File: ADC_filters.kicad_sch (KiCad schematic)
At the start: 9 parts, among them U801 OPA356xxDBV

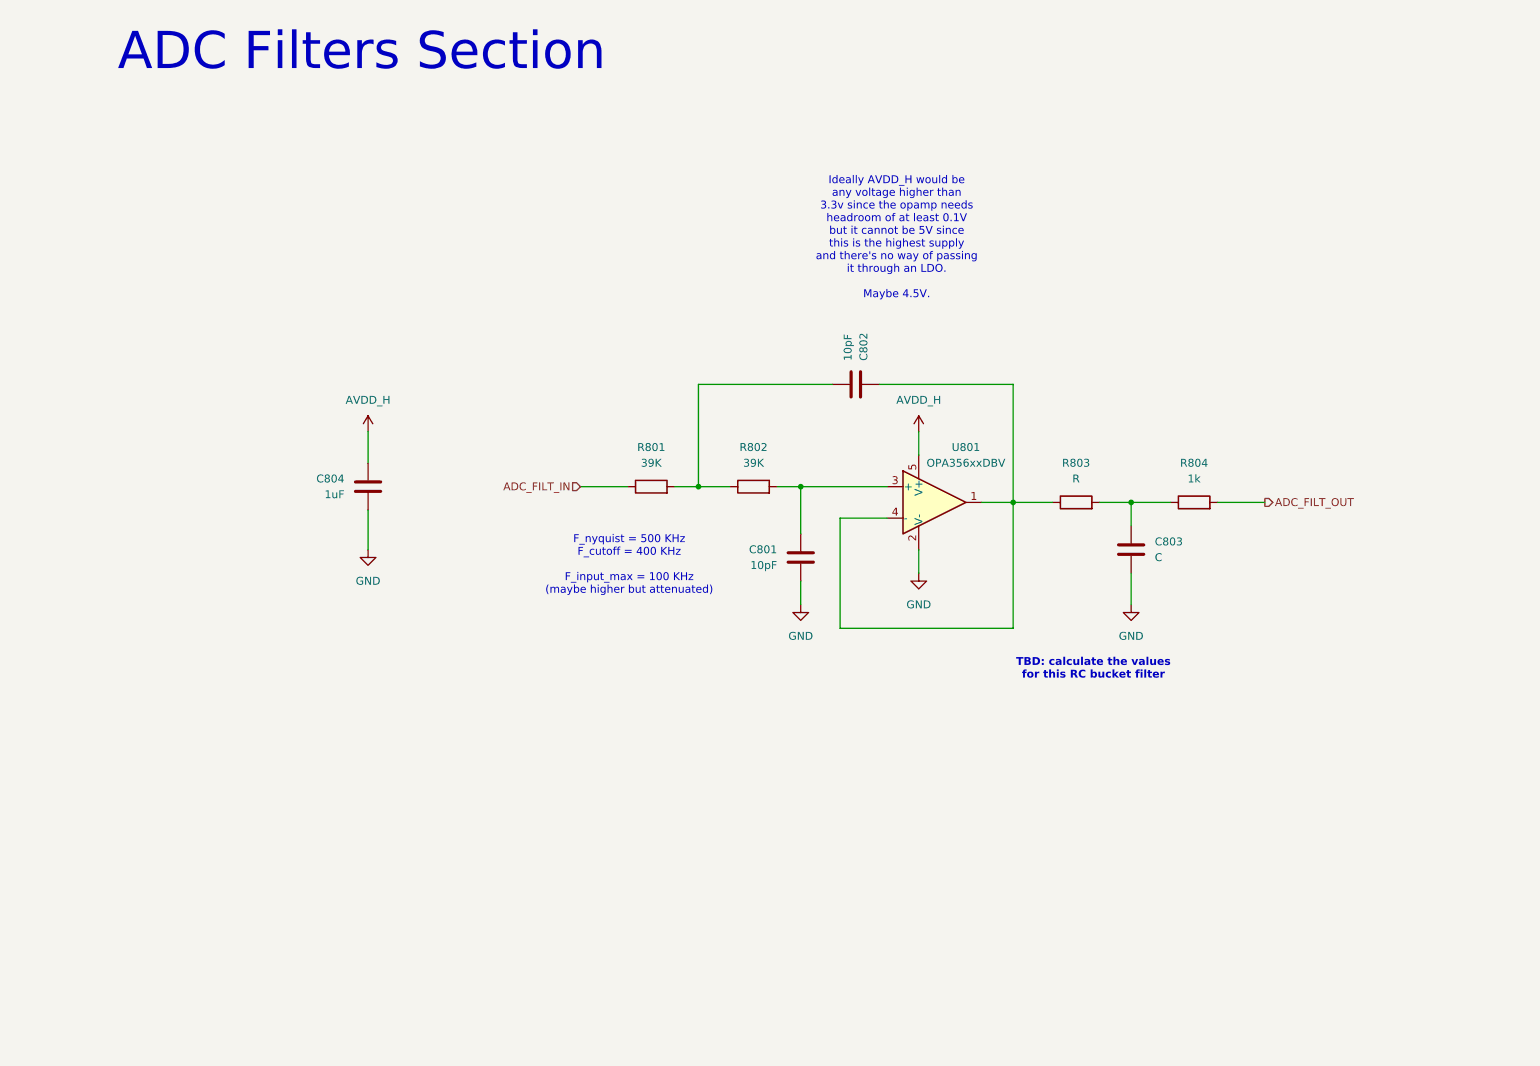
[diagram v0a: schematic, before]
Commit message: 80% done, maybe add more AINs, finish the power circuit and add system & block diagrams
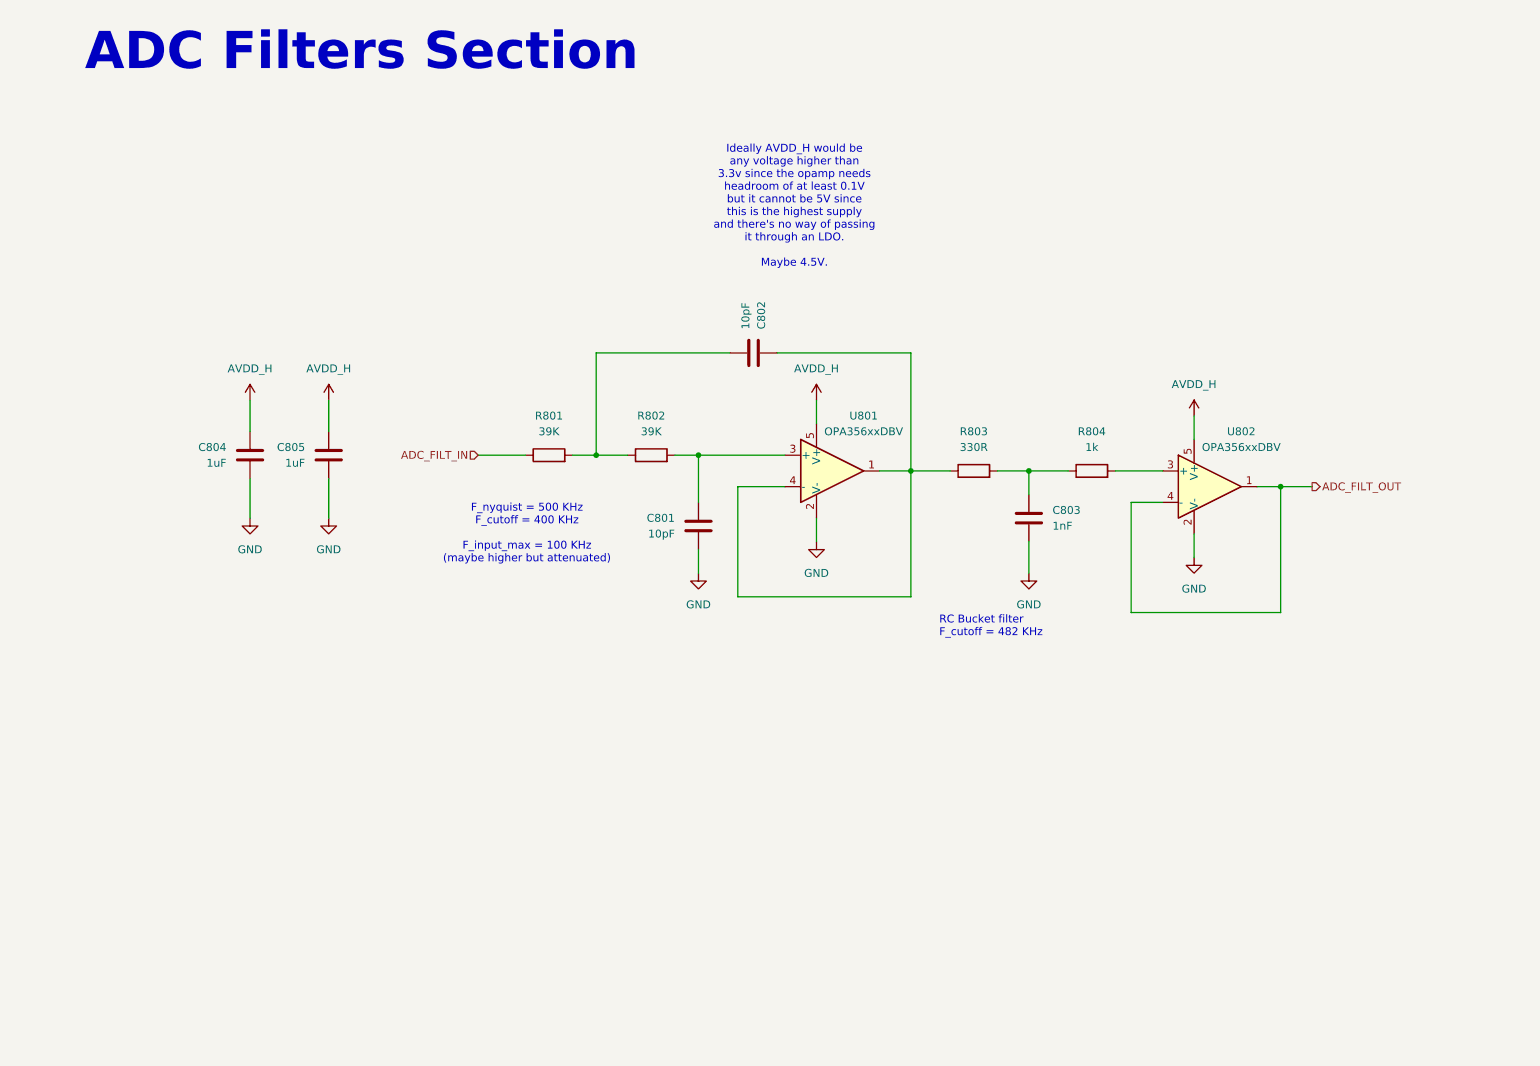
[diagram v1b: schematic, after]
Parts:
- added C805: 1uF, symbol Device:C
- added U802: OPA356xxDBV, Package_TO_SOT_SMD:SOT-23-5, symbol Amplifier_Operational:OPA356xxDBV
- C803: value C -> 1nF
- R803: value R -> 330R
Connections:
- net ADC_FILT_OUT: now also U802.1, U802.4 (-); no longer R804.2
- net AVDD_H: now also C805.1, U802.5 (V+)
- net GND: now also C805.2, U802.2 (V-)
- new net: R804.2, U802.3 (+)
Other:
- note added: "RC Bucket filter F_cutoff = 482 KHz"
- note removed: "TBD: calculate the values for this RC bucket filter"
- moved on the sheet: C801, C802, C803, C804, R801, R802, R803, R804, U801

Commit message: finished individual block placement and started integrating, might need to change the AFEs length
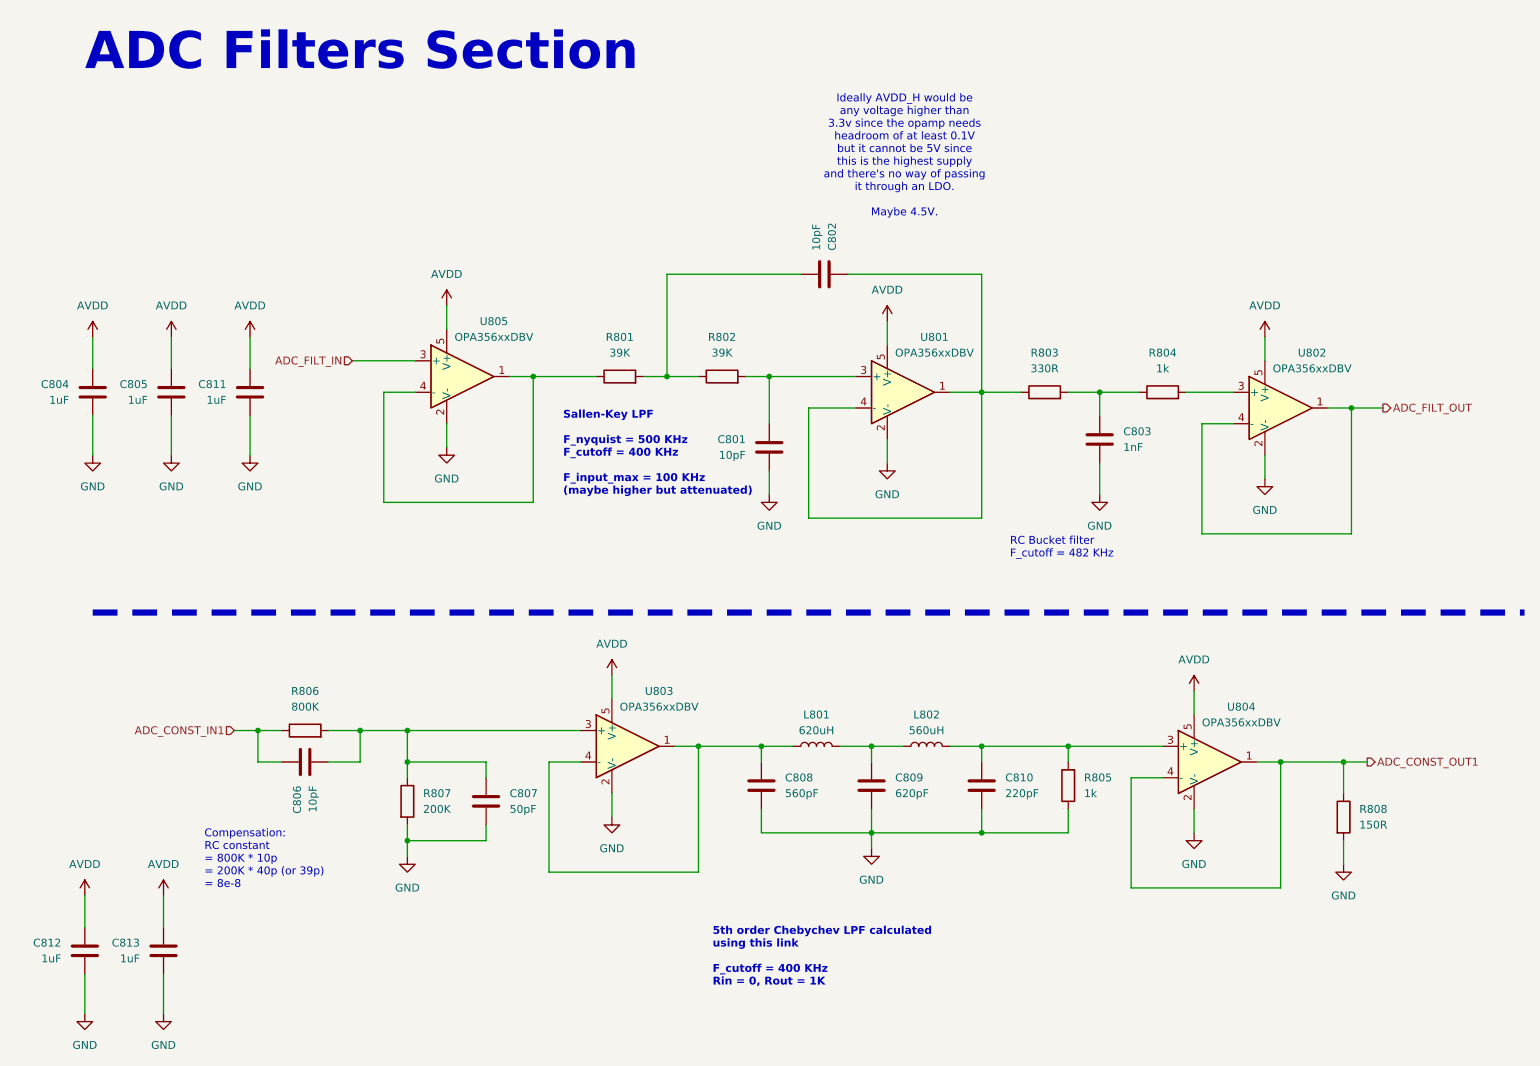
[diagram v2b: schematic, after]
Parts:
- added C806: 10pF, Capacitor_SMD:C_0603_1608Metric, symbol Device:C
- added C807: 50pF, Capacitor_SMD:C_0603_1608Metric, symbol Device:C
- added C808: 560pF, Capacitor_SMD:C_0603_1608Metric, symbol Device:C
- added C809: 620pF, Capacitor_SMD:C_0603_1608Metric, symbol Device:C
- added C810: 220pF, Capacitor_SMD:C_0603_1608Metric, symbol Device:C
- added C811, C812, C813: 1uF, Capacitor_SMD:C_0603_1608Metric, symbol Device:C
- added L801: 620uH, Inductor_SMD:L_1210_3225Metric, symbol Device:L
- added L802: 560uH, Inductor_SMD:L_1210_3225Metric, symbol Device:L
- added R805: 1k, Resistor_SMD:R_0603_1608Metric, symbol Device:R
- added R806: 800K, Resistor_SMD:R_0603_1608Metric, symbol Device:R
- added R807: 200K, Resistor_SMD:R_0603_1608Metric, symbol Device:R
- added R808: 150R, Resistor_SMD:R_0603_1608Metric, symbol Device:R
- added U803, U804, U805: OPA356xxDBV, Package_TO_SOT_SMD:SOT-23-5, symbol Amplifier_Operational:OPA356xxDBV
- C801, C802: footprint (none) -> Capacitor_SMD:C_0603_1608Metric; MPN (none) -> FCC0603N100J500CT
- C803: footprint (none) -> Capacitor_SMD:C_0603_1608Metric; MPN (none) -> CL10B102KB8NNNC
- C804, C805: footprint (none) -> Capacitor_SMD:C_0603_1608Metric; MPN (none) -> 0603X105K250CT
- R801, R802: footprint (none) -> Resistor_SMD:R_0603_1608Metric; MPN (none) -> RT0603BRD0739KL
- R803: footprint (none) -> Resistor_SMD:R_0603_1608Metric; MPN (none) -> TD03G3300BT
- R804: footprint (none) -> Resistor_SMD:R_0603_1608Metric; MPN (none) -> RT0603BRD071KL
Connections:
- net ADC_FILT_IN: now also U805.3 (+); no longer R801.1
- net GND: now also C807.2, C808.2, C809.2, C810.2, C811.2, C812.2, C813.2, R805.1, R807.2, R808.2, U803.2 (V-), U804.2 (V-), U805.2 (V-)
- net AVDD_H renamed AVDD
- net AVDD: now also C811.1, C812.1, C813.1, U803.5 (V+), U804.5 (V+), U805.5 (V+)
- new net: C806.2, C807.1, R806.2, R807.1, U803.3 (+)
- new net: C808.1, L801.1, U803.1, U803.4 (-)
- new net: C810.1, L802.2, R805.2, U804.3 (+)
- new net: C809.1, L801.2, L802.1
- new net: R801.1, U805.1, U805.4 (-)
- new net ADC_CONST_IN1: C806.1, R806.1
- new net ADC_CONST_OUT1: R808.1, U804.1, U804.4 (-)
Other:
- note added: "5th order Chebychev LPF calculated using this link F_cutoff = 400 KHz Rin = 0, Rout = 1K"
- note added: "Compensation: RC constant = 800K * 10p = 200K * 40p (or 39p) = 8e-8"
- note added: "Sallen-Key LPF F_nyquist = 500 KHz F_cutoff = 400 KHz F_input_max = 100 KHz (maybe higher but attenuated)"
- note removed: "F_nyquist = 500 KHz F_cutoff = 400 KHz F_input_max = 100 KHz (maybe higher but attenuated)"
- moved on the sheet: C801, C802, C803, C804, C805, R801, R802, R803, R804, U801, U802
